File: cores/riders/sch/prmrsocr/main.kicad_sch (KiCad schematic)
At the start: 31 parts

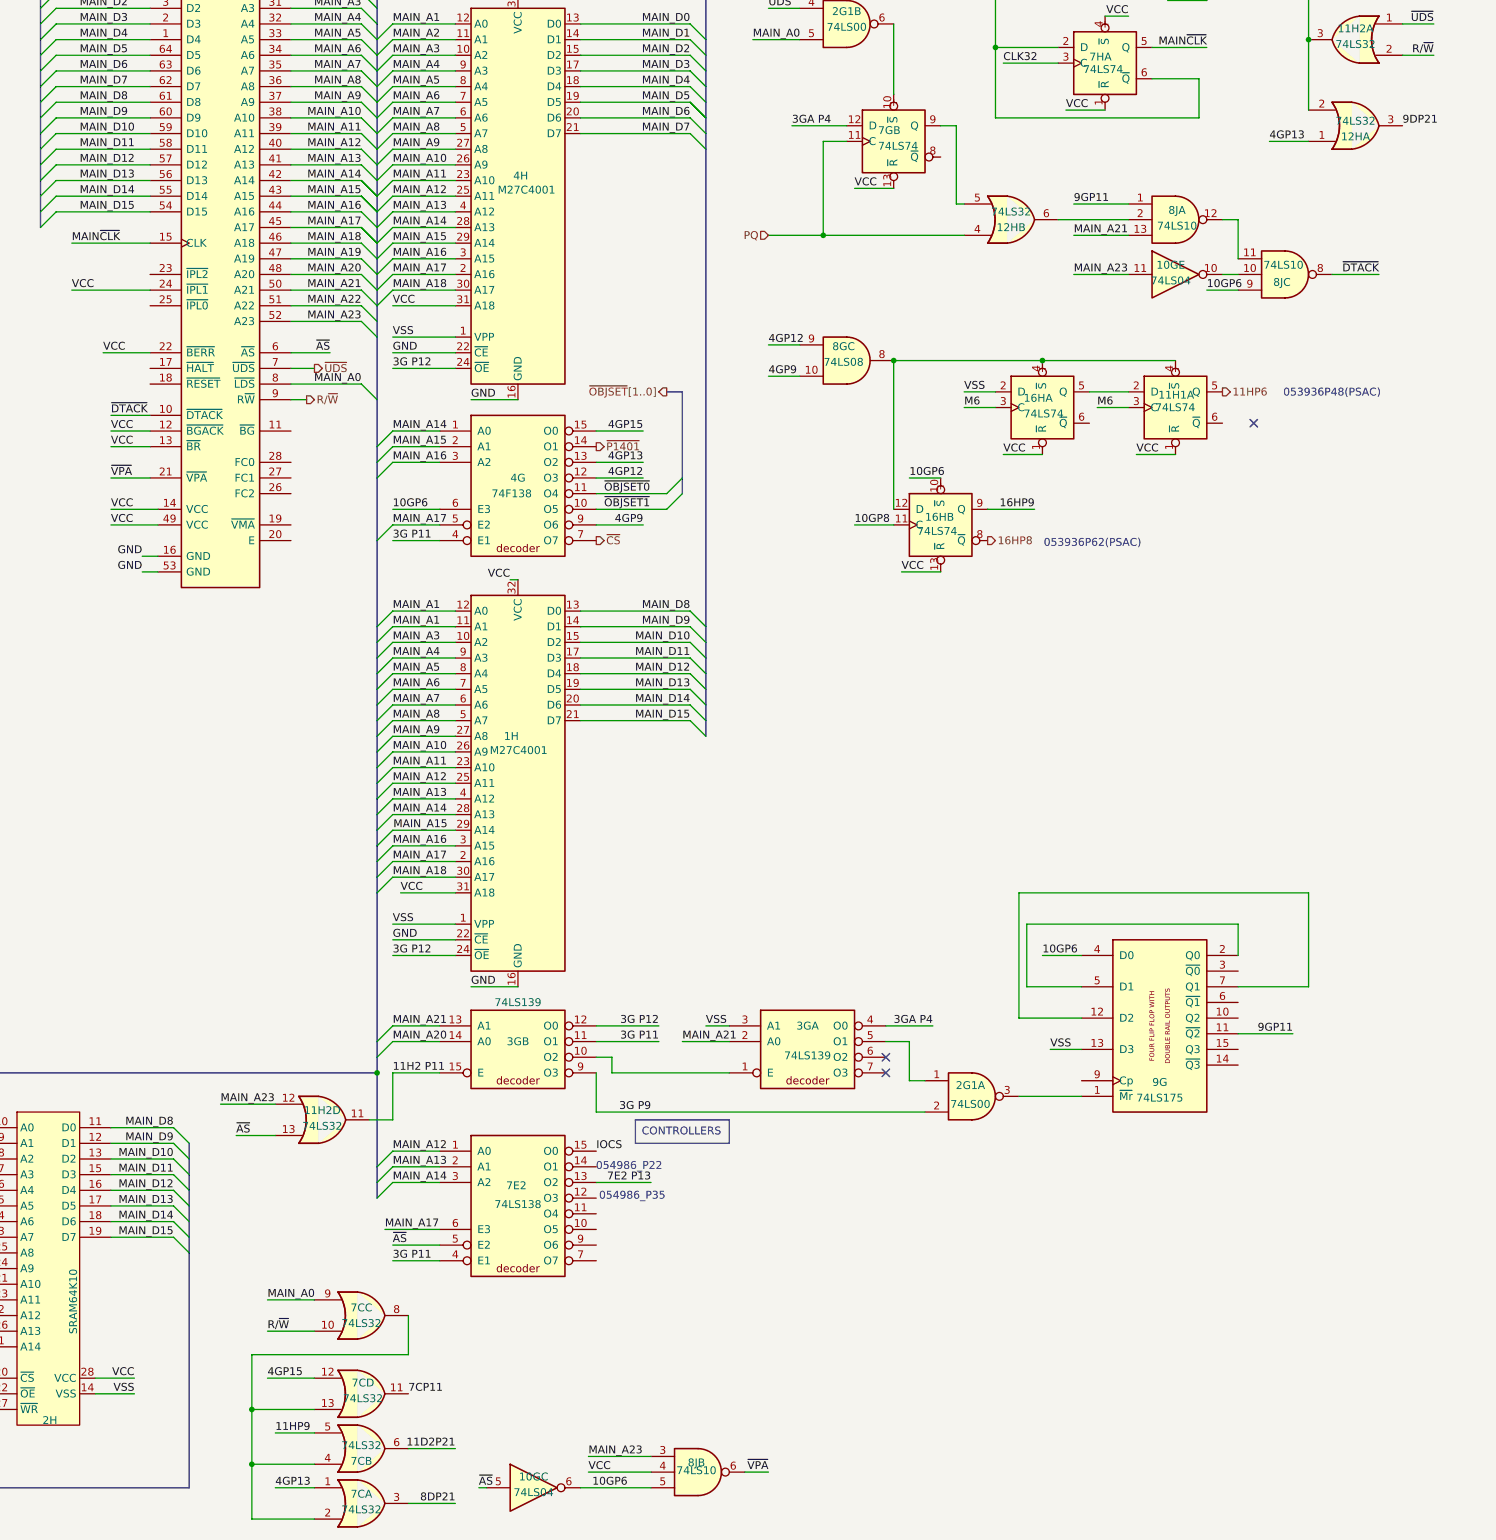
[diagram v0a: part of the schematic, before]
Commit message: sch prmrsocr: psac and colmix revised
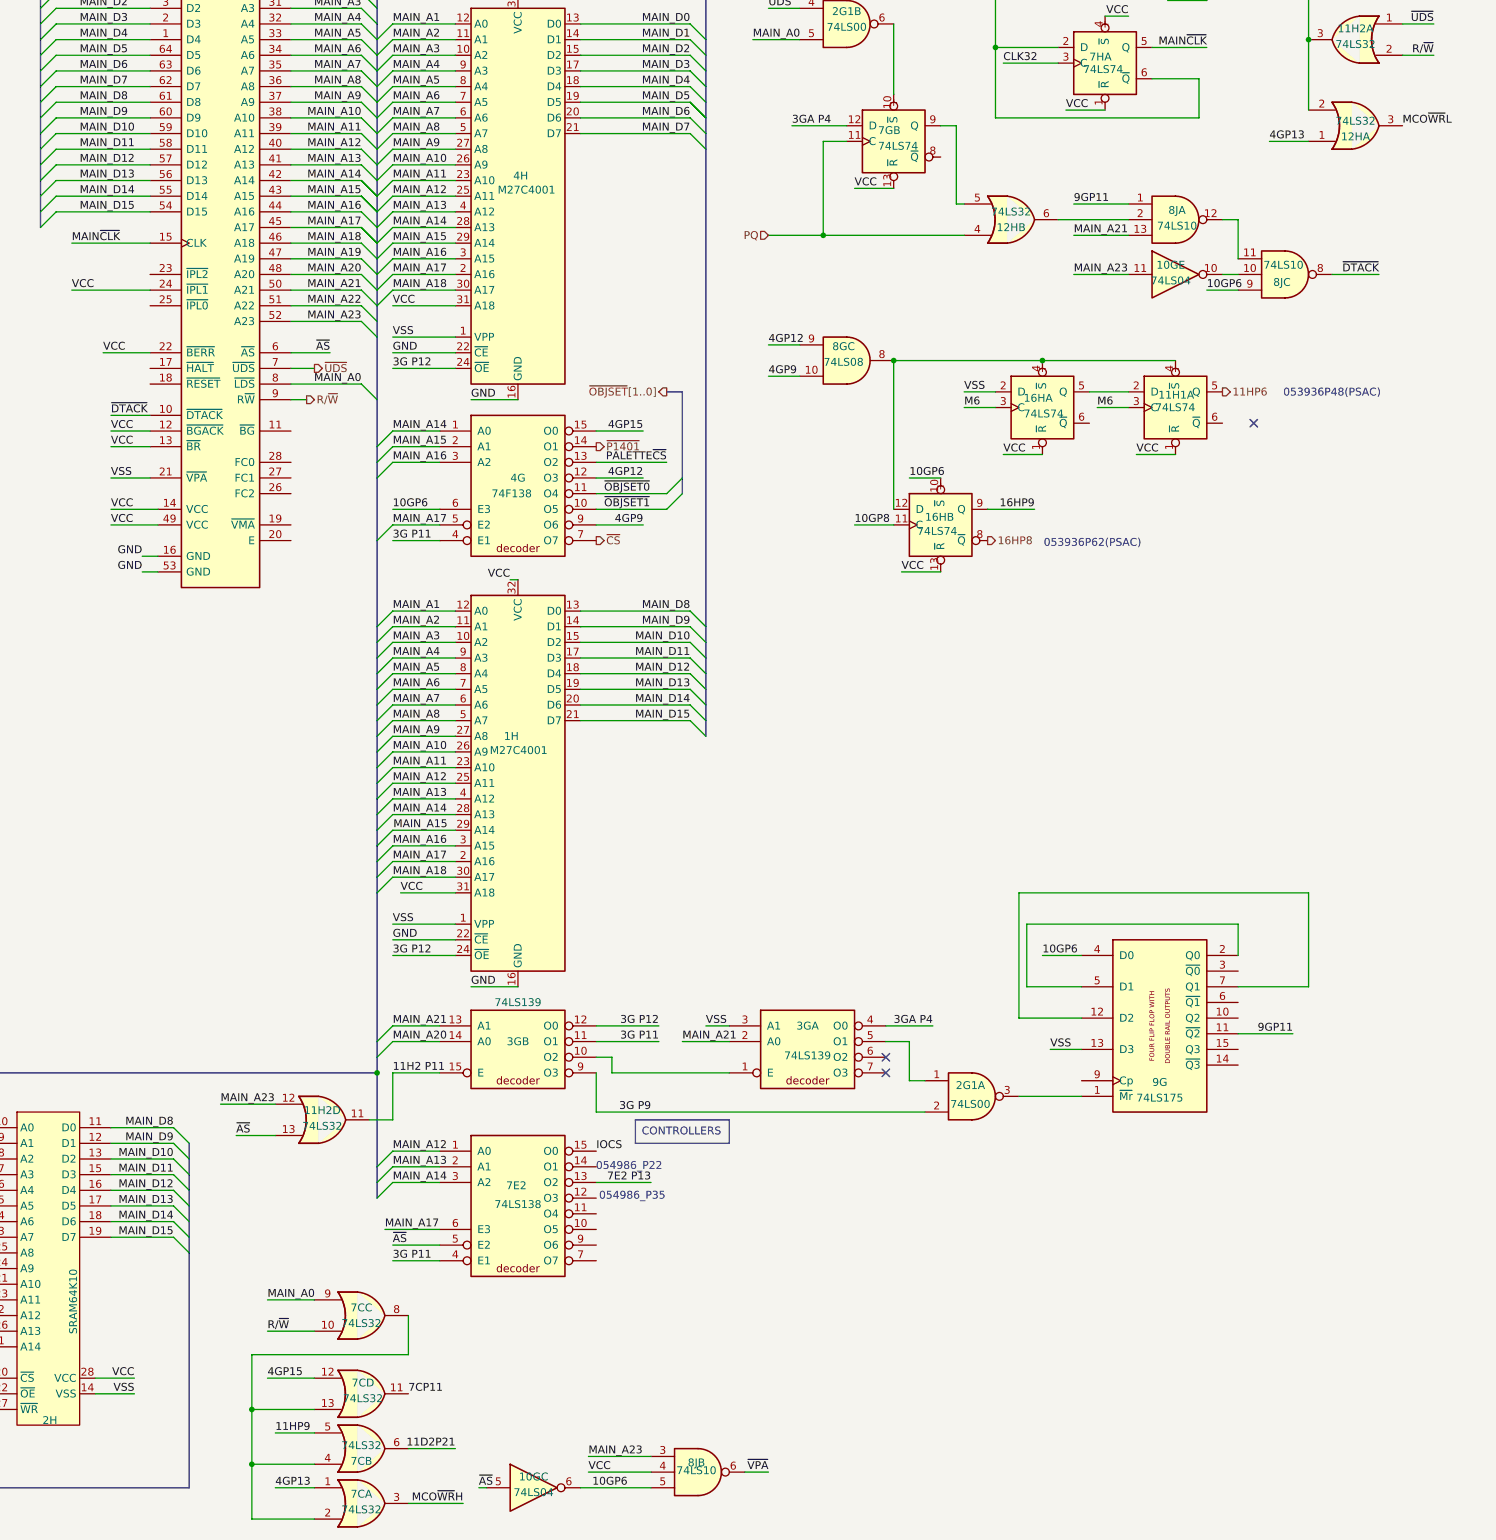
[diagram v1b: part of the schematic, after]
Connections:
- net 4GP13: no longer 4G.13 (O2)
- net MAIN_A1: no longer 1H.11 (A1)
- net MAIN_A2: now also 1H.11 (A1)
- net VSS: now also 6H.21 (~{VPA})
- net ~{VPA}: no longer 6H.21 (~{VPA})
- net 8DP21 renamed MCO~{WR}H
- net 9DP21 renamed MCO~{WR}L
- new net PALETTE~{CS}: 4G.13 (O2)
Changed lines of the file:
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@@
 	(wire
 		(pts
-			(xy 266.7 107.95) (xy 274.32 107.95)
+			(xy 266.7 107.95) (xy 278.13 107.95)
 		)
 		(stroke
@@
 	(wire
 		(pts
+			(xy 245.11 276.86) (xy 236.22 276.86)
+		)
+		(stroke
+			(width 0)
+			(type default)
+		)
+	)
+	(wire
+		(pts
 			(xy 95.25 270.51) (xy 133.35 270.51)
 		)
@@
 	(wire
 		(pts
-			(xy 243.84 276.86) (xy 236.22 276.86)
-		)
-		(stroke
-			(width 0)
-			(type default)
-		)
-	)
-	(wire
-		(pts
 			(xy 179.07 49.53) (xy 194.31 49.53)
 		)
@@
 		)
 	)
+	(label "MCO~{WR}H"
+		(at 245.11 276.86 180)
+		(effects
+			(font
+				(size 1.27 1.27)
+			)
+			(justify right bottom)
+		)
+	)
 	(label "MAIN_A1"
 		(at 233.68 36.83 0)
@@
 		)
 	)
-	(label "4GP13"
-		(at 274.32 107.95 180)
-		(effects
-			(font
-				(size 1.27 1.27)
-			)
-			(justify right bottom)
-		)
-	)
 	(label "~{AS}"
 		(at 247.65 274.32 0)
@@
 		)
 	)
-	(label "MAIN_A1"
+	(label "MAIN_A2"
 		(at 233.68 134.62 0)
 		(effects
@@
 		)
 	)
-	(label "~{VPA}"
+	(label "VSS"
 		(at 187.96 110.49 0)
 		(effects
@@
 		)
 	)
-	(label "9DP21"
+	(label "MCO~{WR}L"
 		(at 397.51 53.34 0)
 		(effects
@@
 		)
 	)
+	(label "PALETTE~{CS}"
+		(at 278.13 107.95 180)
+		(effects
+			(font
+				(size 1.27 1.27)
+			)
+			(justify right bottom)
+		)
+	)
 	(label "3GA P4"
 		(at 20.32 44.45 0)
@@
 		)
 	)
-	(label "8DP21"
-		(at 243.84 276.86 180)
-		(effects
-			(font
-				(size 1.27 1.27)
-			)
-			(justify right bottom)
-		)
-	)

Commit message: wip prmrsocr: Sound
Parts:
- added 7B2: 74LS07, symbol 74xx:74LS07
- added 9E: XTAL_OSC, symbol Device:Crystal_GND23_Small
- added R44: R_Network06_US, Resistor_THT:R_Array_SIP7, symbol Device:R_Network06_US
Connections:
- net 4GP13: no longer 7C.1
- net MAIN~{IRQ}: now also 6H.23 (~{IPL2}), 6H.25 (~{IPL0})
- net PALETTE~{CS}: now also 7C.1
- net VCC: now also 9E.1
- net VSS: now also 9E.4
- net SC_35: now reaches 7E2.12 (O3)
- net SC_22: now reaches 7E2.14 (O1)
- net 7CP8: now reaches 7C.13, 7C.2, 7C.4, 7C.8
- net 3GA P5: now reaches 2G1.1, 3G.5 (O1)
- net at 6H.17 (~{HALT}): now also 7B2.10
- net at 6H.18 (~{RESET}): now also 7B2.8
- net CLK32 renamed 32CLK
- net 32CLK: now also 9E.3
- new net 18CLK: 9E.2
- new net ~{RST}: 7B2.11, 7B2.9
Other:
- note removed: "053936P48(PSAC)"
- note removed: "053936P62(PSAC)"
- note removed: "054986_P22"
- note removed: "054986_P35"
- moved on the sheet: 7CC

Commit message: wip prmrsocr: root
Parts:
- removed 10F, 11F2: 74LS245, symbol jt74:74LS245
- added U41: 74LS04, symbol jt74:74LS04
- renumbered R44 to RA10
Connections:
- net MAIN_A0: now also RA10.5 (R4)
- net R/~{W}: now also RA10.4 (R3), U41.5
- net VCC: now also RA10.1 (common)
- net ~{AS}: now also RA10.7 (R6)
- net ~{RD}: now also U41.6
- net ~{UDS}: now also RA10.6 (R5)
- net ~{VCS}: now reaches 12H.5, 7G.9 (Q)
- net 11HP6 renamed NDTACK
- net 16HP8 renamed NLOE
- no-connect marks 9 -> 15
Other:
- moved on the sheet: 13H, 14H, 7B2D, 7B2E, 7E1A, 7E1B, RA10

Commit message: sch prmrsocr no errors
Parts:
- removed JP3: Jp, symbol Jumper:Jumper_2_Bridged
- removed RA14: 4728 IAM, Resistor_THT:R_Array_SIP9, symbol Device:R_Network08_US
- added 15A: ER5911, symbol arcade:ER5911
- added unit 1 of 7G
- 7H: value 74LS74 -> 74F74
- renumbered U41 to 11G1
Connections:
- net 10GP8 is gone; now on net 11G1P8: 16H.11 (C)
- net 11HP9 is gone; now on net 11H1P9: 7C.5
- net 4GP13 is gone; now on net PALETTE~{CS}: 12H.1
- net VCC: now also 15A.8 (VCC), 7G.1 (~{R}), 7G.4 (~{S})
- net VSS: now also 15A.5 (VSS), 15A.6 (ORG), 7G.3 (C); no longer 6H.21 (~{VPA})
- net ~{HALT}: now also 6H.17 (~{HALT}), 7B2.10, RA10.3 (R2)
- net ~{VPA}: now also 6H.21 (~{VPA})
- net 11H1P9: now reaches 11H1.9 (Q), 12H.12
- net MRESET: now reaches 6H.18 (~{RESET}), 7B2.8
- net MRESET: now also RA10.2 (R1)
- net 11G1P8: now reaches 11G1.8, 11H1.11 (C)
- net 11G1P8: now also 9G.9 (Cp)
- net 7HP6: now reaches 11G1.9, 7H.2 (D), 7H.6 (~{Q})
- net 11D2P21 renamed Z_WE1
- net 16HP9 renamed ZOE
- net 3G P9 renamed 3GP9
- net 3GA P5 renamed 3GA_P5
- net BANK1: no longer names the net of 15C2.5 (Q1)
- net BANK1: now also 15A.1 (CS)
- net MAIN_A22: no longer names the net of 6H.51 (A22)
- net PAL_BANK: no longer names the net of 15C2.7 (Q2)
- net PAL_BANK: now also 15A.2 (CLK)
- net ~{OBJSET0} renamed ~{OBJSET}0
- net ~{OBJSET1} renamed ~{OBJSET}1
- net ~{WRK}: no longer names the net of 15C2.2 (Q0)
- net ~{WRK}: now also 15A.3 (DI)
- new net: 7G.2 (D), 7G.6 (~{Q})
- new net DO: 15A.4 (DO)
- new net S~{CLK}: 7G.5 (Q)
- no-connect marks 15 -> 28
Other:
- note removed: "4.7kΩx8"
- moved on the sheet: 10GC, 10GE, 11G1C, 11G1D, 11H1A, 11H1B, 11H2A, 11H2D, 12HA, 12HB, 12HD, 15H2D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
